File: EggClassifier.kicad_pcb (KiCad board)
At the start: 2 copper layers, 100 x 100 mm, 77 parts, among them J1 ST-LINK, J10 LCD_CHAR, J11 SERVO2, J12 BME280, J13 UART1, J14 FAN, J15 UART2, J16 AS7265X, J17 TFT_SPI, J2 USB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

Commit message: snapshot
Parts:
- C10, C11, C14, C15, C2, C5, C6, C7, C8, C9: footprint Capacitor_SMD:C_0805_2012Metric_Pad1.18x1.45mm_HandSolder -> EggClassifier:C_0805_2012Metric_Pad1.18x1.45mm_HandSolder
- C12, C13, C16, C17, C18, C19, C20, C21, C22: footprint Capacitor_SMD:C_0603_1608Metric_Pad1.08x0.95mm_HandSolder -> EggClassifier:C_0805_2012Metric_Pad1.18x1.45mm_HandSolder
- D1: footprint Diode_SMD:D_SMB_Handsoldering -> EggClassifier:D_SMB_Handsoldering
- D2, D3, D4: footprint Diode_SMD:D_SMA_Handsoldering -> EggClassifier:D_SMA_Handsoldering
- D5, D6: footprint LED_SMD:LED_0805_2012Metric_Pad1.15x1.40mm_HandSolder -> EggClassifier:LED_0805_2012Metric_Pad1.15x1.40mm_HandSolder
- H1, H2, H3, H4: footprint PCM_JLCPCB:Hole, 3mm -> EggClassifier:Hole, 3mm
- J1: footprint Connector_PinHeader_2.54mm:PinHeader_1x05_P2.54mm_Vertical -> EggClassifier:PinHeader_1x05_P2.54mm_Vertical
- J10, J12, J16, J2, J5: footprint Connector_PinHeader_2.54mm:PinHeader_1x04_P2.54mm_Vertical -> EggClassifier:PinHeader_1x04_P2.54mm_Vertical
- J11, J13, J14, J15, J8, J9: footprint Connector_PinHeader_2.54mm:PinHeader_1x03_P2.54mm_Vertical -> EggClassifier:PinHeader_1x03_P2.54mm_Vertical
- J17: footprint Connector_PinHeader_2.54mm:PinHeader_1x15_P2.54mm_Vertical -> EggClassifier:PinSocket_1x14_P2.54mm_Vertical
- J6: footprint Connector_PinHeader_2.54mm:PinHeader_2x09_P2.54mm_Vertical -> EggClassifier:PinHeader_2x09_P2.54mm_Vertical
- J7: footprint Connector_PinHeader_2.54mm:PinHeader_2x05_P2.54mm_Vertical -> EggClassifier:PinHeader_2x05_P2.54mm_Vertical
- Q1, Q2, Q3: footprint PCM_Package_TO_SOT_SMD_AKL:SOT-223-3_TabPin2 -> EggClassifier:SOT-223-3_TabPin2
- R1, R10, R11, R12, R13, R14, R15, R16, R17, R18, R19, R2, R20, R3, R4, R5, R6, R7, R8, R9: footprint Resistor_SMD:R_0805_2012Metric_Pad1.20x1.40mm_HandSolder -> EggClassifier:R_0805_2012Metric_Pad1.20x1.40mm_HandSolder
- SW1: footprint Button_Switch_THT:SW_PUSH_6mm_H4.3mm -> EggClassifier:SW_PUSH_6mm_H4.3mm
- U1: footprint LM2676S-3.3_NOPB:TO127P1435X464-8N -> EggClassifier:TO127P1435X464-8N
- U2: footprint Package_TO_SOT_SMD:SOT-223-3_TabPin2 -> EggClassifier:SOT-223-3_TabPin2
- U3: footprint Package_QFP:LQFP-100_14x14mm_P0.5mm -> EggClassifier:LQFP-100_14x14mm_P0.5mm
- U4: footprint PCM_JLCPCB:SOIC-8_L5.3-W5.3-P1.27-LS8.0-BL -> EggClassifier:SOIC-8_L5.3-W5.3-P1.27-LS8.0-BL
- Y1: footprint Oscillator:Oscillator_SMD_Abracon_ASV-4Pin_7.0x5.1mm_HandSoldering -> EggClassifier:Oscillator_SMD_Abracon_ASV-4Pin_7.0x5.1mm_HandSoldering
- moved R13 4.40 mm to (117.5, 69.0)
- moved R3 1.45 mm to (104.3, 55.8)
- moved R4 1.45 mm to (107.7, 55.8)
- moved J12 1.30 mm to (99.8, 51.4)
- moved J15 1.27 mm to (142.5, 51.4)
- moved C17 0.64 mm to (124.6, 72.3)
- moved C19 0.42 mm to (123.6, 96.6)
- moved C22 0.18 mm to (143.8, 77.5)
- moved C20 0.17 mm to (138.7, 98.0)
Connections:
- J7 pad 9: GND -> VCC
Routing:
- net UART2_TX: track 0.00 -> 76.0 mm, vias 0 -> 1
- net USER_GPIO4: track 0.00 -> 72.3 mm, vias 0 -> 3
- net USER_GPIO1: track 0.00 -> 55.0 mm, vias 0 -> 1
- net USER_GPIO2: track 0.00 -> 54.9 mm, vias 0 -> 1
- net USER_GPIO3: track 0.00 -> 54.3 mm, vias 0 -> 1
- net +3.3V: track 139.7 -> 159.2 mm, vias 5 -> 8
- net I2C1_SDA: track 47.2 -> 55.9 mm
- net I2C1_SCL: track 46.6 -> 54.2 mm
- net VCC: track 211.9 -> 218.9 mm
- net Net-(Y1-OUT): track 4.61 -> 9.26 mm
- net UART1_TX: track 49.5 -> 53.8 mm
- net Net-(U3-PH0): track 25.4 -> 22.1 mm
- net UART1_RX: track 47.6 -> 50.3 mm
- net GND: track 85.2 -> 87.8 mm
- net UART2_RX: track 33.3 -> 32.1 mm
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
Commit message: almost finsihed
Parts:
- moved R9 2.29 mm to (92.7, 61.6)
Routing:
- net ADC_IN2: track 0.00 -> 71.6 mm, vias 0 -> 1
- net ADC_IN1: track 0.00 -> 65.0 mm, vias 0 -> 1
- net I2C2_SDA: track 78.5 -> 105.9 mm
- net I2C2_SCL: track 79.3 -> 97.8 mm
- net +3.3V: track 159.2 -> 161.6 mm
- net I2C1_SDA: track 55.9 -> 55.2 mm

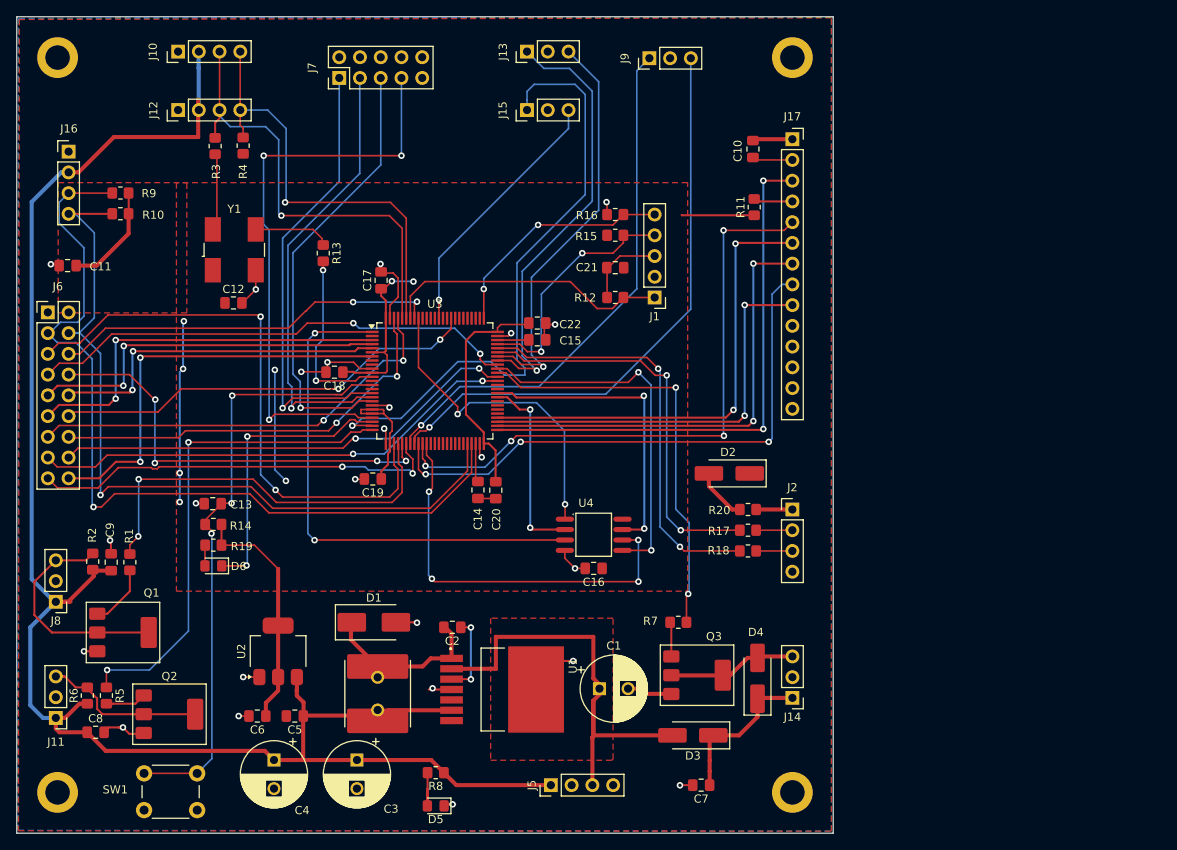
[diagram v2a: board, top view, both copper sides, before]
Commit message: complete PCB layout
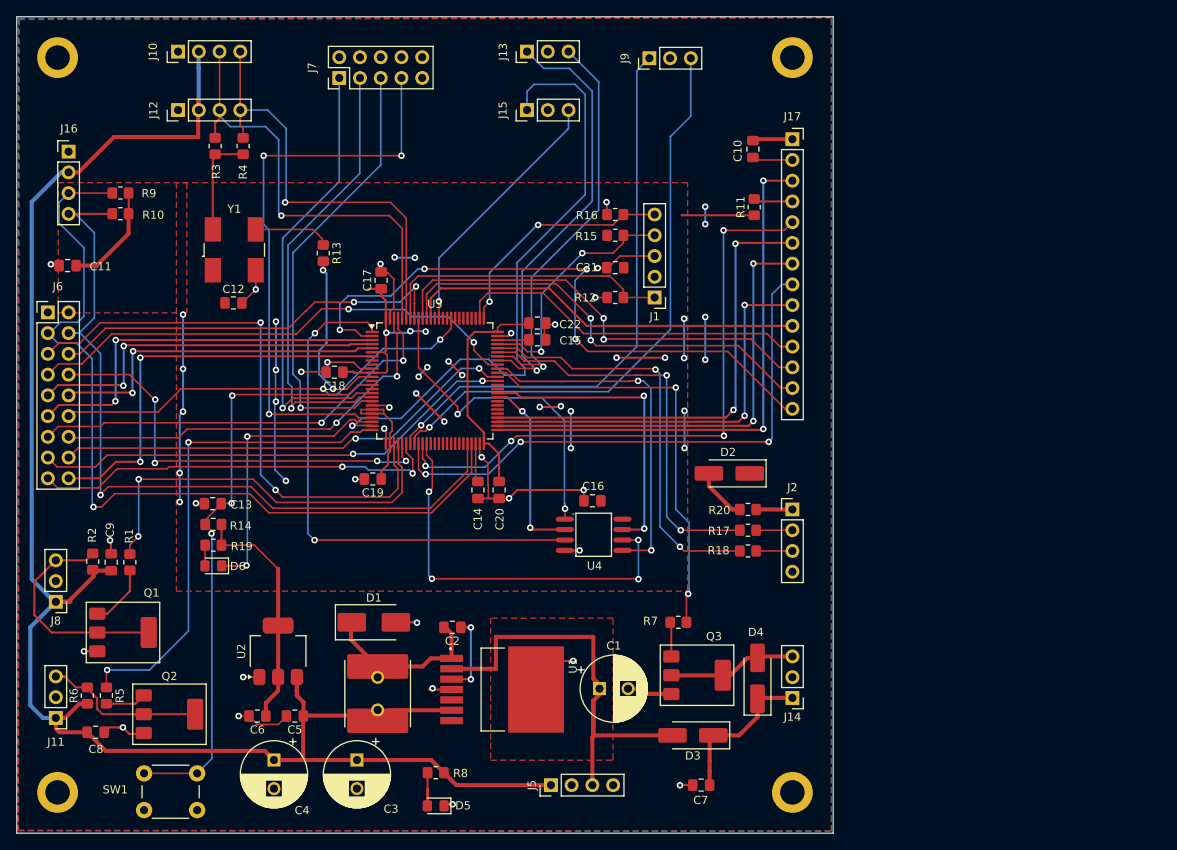
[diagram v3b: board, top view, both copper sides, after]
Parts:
- moved C16 8.28 mm to (150.5, 99.3)
- moved C20 0.41 mm to (139.1, 98.0)
- moved R4 0.05 mm to (107.7, 55.8)
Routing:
- net TFT_INT: track 0.00 -> 78.8 mm, vias 0 -> 4
- net SPI1_MOSI: track 0.00 -> 55.2 mm, vias 0 -> 2
- net SPI1_MISO: track 0.00 -> 55.1 mm, vias 0 -> 2
- net SPI1_SCK: track 0.00 -> 49.1 mm
- net SPI1_NCS: track 0.00 -> 43.5 mm
- net GND: track 87.8 -> 123.0 mm, vias 24 -> 36
- net +3.3V: track 161.6 -> 193.0 mm, vias 8 -> 22
- net VCC: track 218.7 -> 226.1 mm, vias 0 -> 4
- net ADC_IN1: track 65.0 -> 69.1 mm
- net CAM_VS: track 47.5 -> 50.0 mm
- net CAM_MCLK: track 60.2 -> 62.0 mm
- net /DevEBox/QSPI_D2: track 63.8 -> 65.1 mm
- net /DevEBox/QSPI_D0: track 44.5 -> 43.2 mm
- net /DevEBox/QSPI_NCS: track 39.7 -> 40.9 mm
- net CAM_HS: track 71.6 -> 70.4 mm
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
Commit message: more fine tuning
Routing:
- net UART2_TX: track 76.3 -> 70.6 mm
- net VCC: track 226.1 -> 231.2 mm, vias 4 -> 6
- net /DevEBox/QSPI_CLK: track 49.2 -> 46.7 mm
- net I2C2_SCL: track 97.8 -> 95.9 mm
- net I2C2_SDA: track 105.7 -> 103.9 mm
- net /DevEBox/QSPI_D3: track 37.2 -> 35.6 mm
- net /DevEBox/DM: track 48.9 -> 49.9 mm
- net /DevEBox/QSPI_D1: track 22.8 -> 21.9 mm
- net GND: track 123.0 -> 123.5 mm

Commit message: more fine tuning
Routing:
- net GND: track 123.5 -> 124.5 mm
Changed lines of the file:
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@@
 	)
 	(segment
+		(start 128.6918 85.8978)
+		(end 132.3748 89.5808)
+		(width 0.25)
+		(layer "F.Cu")
+		(net 1)
+	)
+	(segment
 		(start 156.9366 122.931)
 		(end 156.3016 122.296)
@@
 	)
 	(segment
-		(start 134.5592 83.8912)
-		(end 132.832 82.164)
-		(width 0.25)
-		(layer "F.Cu")
-		(net 1)
-	)
-	(segment
 		(start 129.022 114.2188)
 		(end 128.7172 114.2188)
@@
 	)
 	(segment
-		(start 132.3748 89.5808)
-		(end 128.9204 86.1264)
+		(start 132.832 82.164)
+		(end 134.5592 83.8912)
 		(width 0.25)
 		(layer "F.Cu")
@@
 	)
 	(segment
+		(start 128.5648 85.8978)
+		(end 128.6918 85.8978)
+		(width 0.25)
+		(layer "F.Cu")
+		(net 1)
+	)
+	(segment
 		(start 162.7925 134.112)
 		(end 161.2496 134.112)
@@
 	)
 	(segment
-		(start 132.832 82.164)
-		(end 132.7558 82.164)
-		(width 0.25)
-		(layer "F.Cu")
-		(net 1)
-	)
-	(segment
 		(start 137.7596 94.7624)
 		(end 137.7596 99.0003)
@@
 	)
 	(segment
+		(start 128.4378 85.7708)
+		(end 128.5648 85.8978)
+		(width 0.25)
+		(layer "F.Cu")
+		(net 1)
+	)
+	(segment
+		(start 132.8066 82.164)
+		(end 132.832 82.164)
+		(width 0.25)
+		(layer "F.Cu")
+		(net 1)
+	)
+	(segment
 		(start 140.2781 99.0003)
 		(end 140.2996 98.9788)
@@
 	)
 	(segment
+		(start 132.4764 81.8338)
+		(end 132.8066 82.164)
+		(width 0.25)
+		(layer "F.Cu")
+		(net 1)
+	)
+	(segment
 		(start 133.731 136.462)
 		(end 132.153 136.462)
@@
 	)
 	(via
-		(at 128.9204 86.1264)
+		(at 128.4378 85.7708)
 		(size 0.8)
 		(drill 0.4)
@@
 	)
 	(via
-		(at 132.7558 82.164)
+		(at 132.4764 81.8338)
 		(size 0.8)
 		(drill 0.4)
@@
 	)
 	(segment
-		(start 124.8818 93.5432)
+		(start 121.1988 93.5432)
+		(end 121.9608 92.7812)
+		(width 0.2)
+		(layer "B.Cu")
+		(net 35)
+	)
+	(segment
+		(start 125.6438 92.7812)
 		(end 133.7718 84.6532)
 		(width 0.2)
@@
 	)
 	(segment
-		(start 121.1988 93.5432)
-		(end 124.8818 93.5432)
+		(start 121.9608 92.7812)
+		(end 125.6438 92.7812)
 		(width 0.2)
 		(layer "B.Cu")
@@
 	)
 	(segment
-		(start 127.0662 89.1998)
-		(end 134.4322 81.8338)
+		(start 139.055 81.5544)
+		(end 141.3664 79.243)
 		(width 0.2)
 		(layer "B.Cu")
@@
 	)
 	(segment
-		(start 121.096875 90.088475)
-		(end 121.351525 90.088475)
+		(start 142.484 50.16)
+		(end 142.499 50.175)
 		(width 0.2)
 		(layer "B.Cu")
@@
 	)
 	(segment
-		(start 142.484 50.16)
-		(end 142.499 50.175)
+		(start 149.6214 49.525)
+		(end 148.3768 48.2804)
 		(width 0.2)
 		(layer "B.Cu")
@@
 	)
 	(segment
-		(start 142.499 50.175)
-		(end 142.499 51.43)
+		(start 149.6214 62.6568)
+		(end 149.6214 49.525)
 		(width 0.2)
 		(layer "B.Cu")
@@
 	)
 	(segment
-		(start 148.3768 48.2804)
-		(end 143.373 48.2804)
+		(start 121.7322 89.4792)
+		(end 126.3296 89.4792)
 		(width 0.2)
 		(layer "B.Cu")
@@
 	)
 	(segment
-		(start 149.6214 62.6568)
-		(end 149.6214 49.525)
+		(start 142.499 50.175)
+		(end 142.499 51.43)
 		(width 0.2)
 		(layer "B.Cu")
@@
 	)
 	(segment
-		(start 149.6214 49.525)
-		(end 148.3768 48.2804)
+		(start 143.373 48.2804)
+		(end 142.499 49.1544)
 		(width 0.2)
 		(layer "B.Cu")
@@
 	)
 	(segment
-		(start 134.4322 81.8338)
-		(end 138.7756 81.8338)
+		(start 142.499 49.1544)
+		(end 142.499 50.16)
 		(width 0.2)
 		(layer "B.Cu")
@@
 	)
 	(segment
-		(start 122.2402 89.1998)
-		(end 127.0662 89.1998)
+		(start 121.122925 90.088475)
+		(end 121.7322 89.4792)
 		(width 0.2)
 		(layer "B.Cu")
@@
 	)
 	(segment
-		(start 141.3664 79.243)
-		(end 141.3664 70.9118)
+		(start 121.096875 90.088475)
+		(end 121.122925 90.088475)
 		(width 0.2)
 		(layer "B.Cu")
@@
 	)
 	(segment
-		(start 142.499 50.16)
-		(end 142.484 50.16)
+		(start 141.3664 79.243)
+		(end 141.3664 70.9118)
 		(width 0.2)
 		(layer "B.Cu")
@@
 	)
 	(segment
-		(start 142.499 49.1544)
-		(end 142.499 50.16)
+		(start 134.2544 81.5544)
+		(end 139.055 81.5544)
 		(width 0.2)
 		(layer "B.Cu")
@@
 	)
 	(segment
-		(start 121.351525 90.088475)
-		(end 122.2402 89.1998)
+		(start 148.3768 48.2804)
+		(end 143.373 48.2804)
 		(width 0.2)
 		(layer "B.Cu")
@@
 	)
 	(segment
-		(start 138.7756 81.8338)
-		(end 141.3664 79.243)
+		(start 142.499 50.16)
+		(end 142.484 50.16)
 		(width 0.2)
 		(layer "B.Cu")
@@
 	)
 	(segment
-		(start 143.373 48.2804)
-		(end 142.499 49.1544)
+		(start 126.3296 89.4792)
+		(end 134.2544 81.5544)
 		(width 0.2)
 		(layer "B.Cu")

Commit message: yet more tweaks
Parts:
- J5: footprint EggClassifier:PinHeader_1x04_P2.54mm_Vertical -> EggClassifier:TerminalBlock_Xinya_XY308-2.54-4P_1x04_P2.54mm_Horizontal
- moved C12 9.17 mm to (105.9, 65.9)
- moved Y1 3.57 mm to (105.9, 72.0)
- moved R13 2.80 mm to (117.9, 71.7)
- turned J5 to 0 degrees
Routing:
- net VCC: track 231.2 -> 214.8 mm, vias 6 -> 7
- net Net-(J11-Pin_3): track 22.4 -> 25.4 mm, vias 0 -> 1
- net Net-(U3-PH0): track 22.3 -> 19.4 mm
- net USER_GPIO1: track 55.0 -> 53.6 mm
- net GND: track 124.5 -> 123.2 mm, vias 36 -> 37
- net CAM_HS: track 70.4 -> 69.5 mm
- net Net-(Q2-B): track 4.28 -> 4.99 mm
- net Net-(Y1-OUT): track 9.26 -> 9.96 mm
- net Net-(J8-Pin_3): vias 0 -> 1

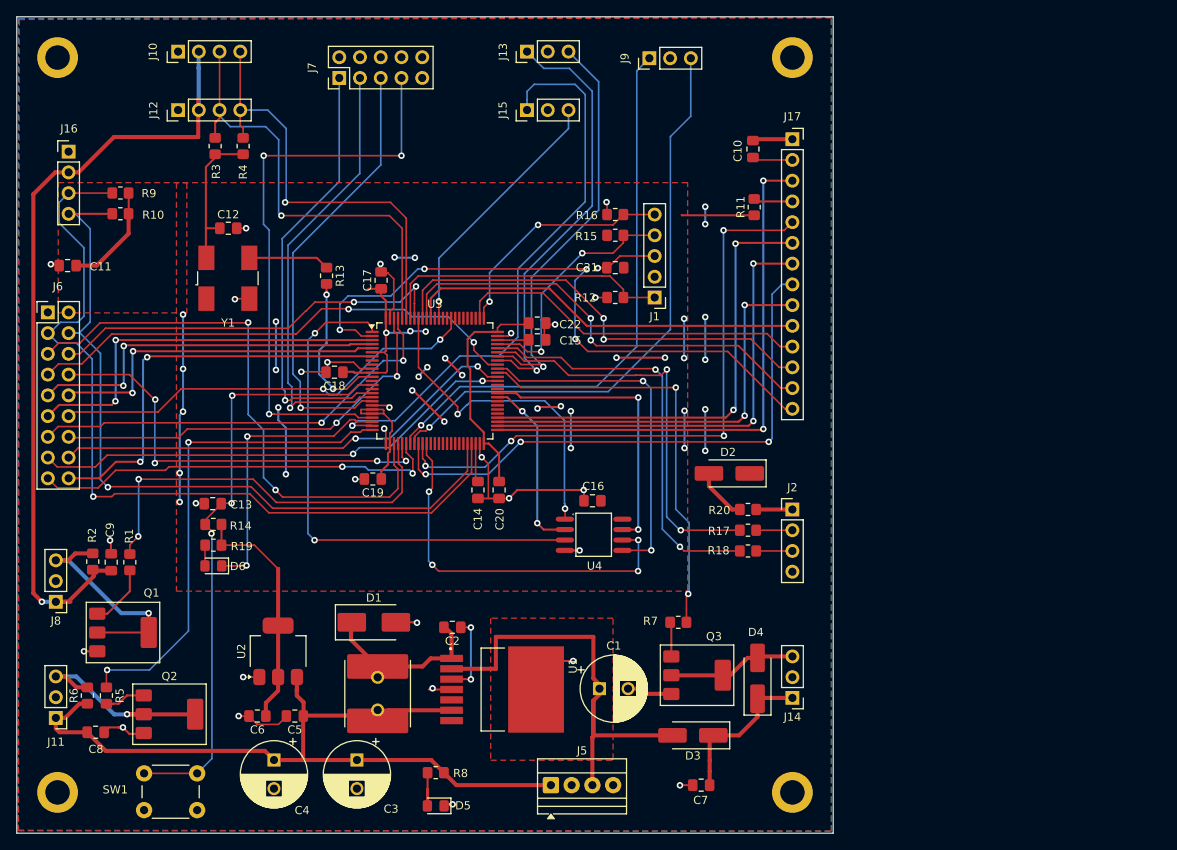
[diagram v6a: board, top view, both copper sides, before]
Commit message: change board to dimensions 120mm x 80mm
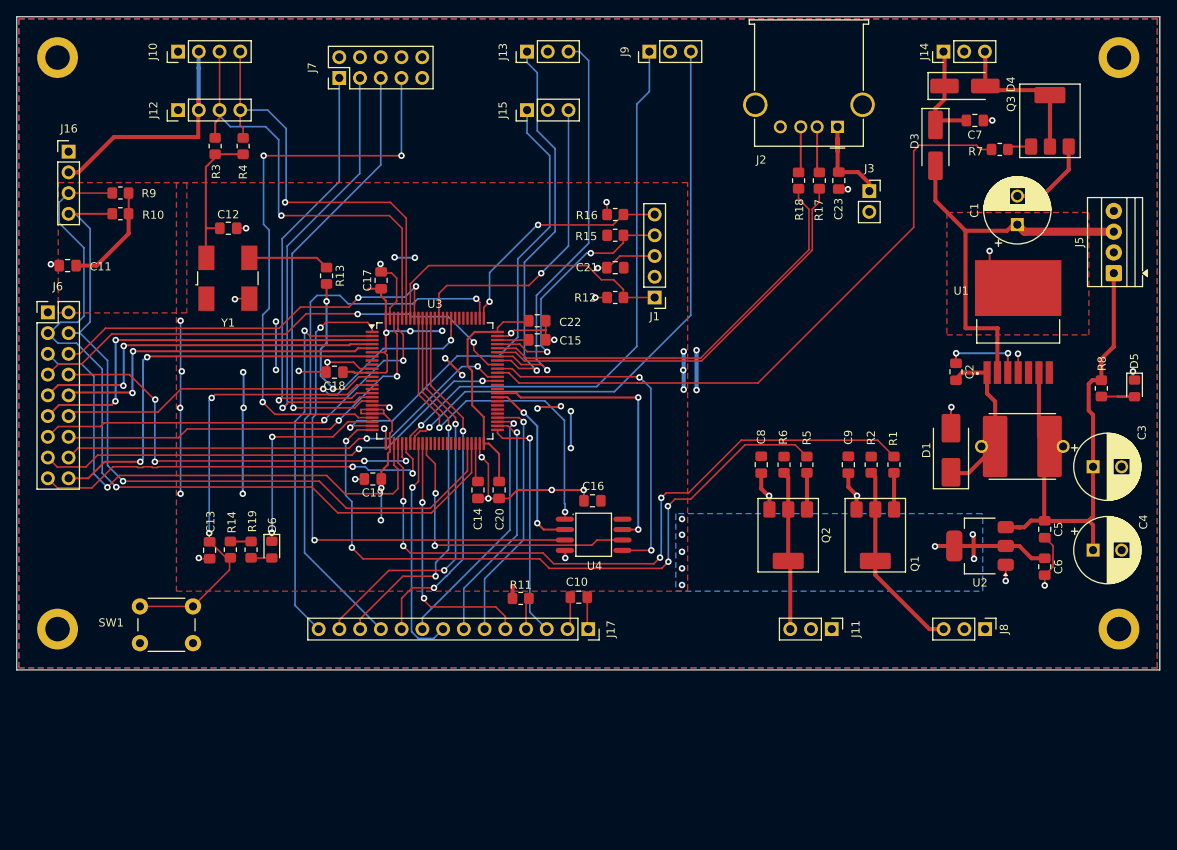
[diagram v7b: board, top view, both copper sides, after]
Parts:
- removed D2: SS36, EggClassifier:D_SMA_Handsoldering
- removed R20: 0, EggClassifier:R_0805_2012Metric_Pad1.20x1.40mm_HandSolder
- added C23: 104, EggClassifier:C_0805_2012Metric_Pad1.18x1.45mm_HandSolder, F.Cu at (180.7, 60.1)
- added J3: Jumper, EggClassifier:PinSocket_1x02_P2.54mm_Vertical, F.Cu at (184.4, 61.4)
- J2: value USB -> USB_A; footprint EggClassifier:PinHeader_1x04_P2.54mm_Vertical -> EggClassifier:USB_A_Molex_67643_Horizontal
- moved J8 113.9 mm to (198.6, 115.0), turned to -90 degrees
- moved C4 103.6 mm to (211.8, 105.3), turned to 0 degrees
- moved D5 99.7 mm to (216.9, 85.5), turned to -90 degrees
- moved C6 98.1 mm to (205.9, 107.4), turned to -90 degrees
- moved C3 97.1 mm to (211.8, 95.1), turned to 0 degrees
- moved R2 96.1 mm to (184.6, 94.9), turned to -90 degrees
- moved J11 95.7 mm to (179.8, 115.0), turned to -90 degrees
- moved C5 94.6 mm to (205.9, 102.8), turned to -90 degrees
- moved R1 94.3 mm to (187.4, 94.9)
- moved R8 94.1 mm to (212.8, 85.5), turned to -90 degrees
- moved J5 93.2 mm to (214.4, 71.4), turned to 90 degrees
- moved Q1 92.9 mm to (185.2, 103.5), turned to -90 degrees
- moved C9 91.1 mm to (181.9, 94.9), turned to -90 degrees
- moved R5 90.3 mm to (176.8, 94.9)
- moved R6 89.9 mm to (174.0, 94.9), turned to -90 degrees
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- renumbered R18 to R17, R17 to R18
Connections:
- J2 pad 1: Net-(J2-Pin_1) -> +5V
- J2 pad 2: Net-(J2-Pin_2) -> Net-(J2-D-)
- J2 pad 3: Net-(J2-Pin_3) -> Net-(J2-D+)
- R17 pad 1: /DevEBox/DP -> /DevEBox/DM
- R17 pad 2: Net-(J2-Pin_3) -> Net-(J2-D-)
- R18 pad 1: /DevEBox/DM -> /DevEBox/DP
- R18 pad 2: Net-(J2-Pin_2) -> Net-(J2-D+)
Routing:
- net VCC: track 214.8 -> 104.0 mm, vias 7 -> 2
- net TFT_RS: track 75.1 -> 31.6 mm, vias 4 -> 2
- net TFT_BL: track 69.2 -> 28.1 mm, vias 3 -> 1
- net SPI2_NCS: track 66.6 -> 28.9 mm, vias 2 -> 1
- net SERVO_OUT1: track 49.7 -> 85.1 mm, vias 2 -> 4
- net TFT_INT: track 78.8 -> 46.8 mm, vias 4 -> 1
- net FAN_OUT: track 52.1 -> 78.8 mm, vias 2 -> 0
- net SPI2_SCK: track 55.7 -> 29.5 mm, vias 2 -> 1
- net SPI2_MOSI: track 56.8 -> 30.8 mm, vias 2 -> 1
- net SPI1_NCS: track 43.5 -> 68.1 mm, vias 0 -> 1
- net SERVO_OUT2: track 60.3 -> 84.9 mm, vias 2 -> 4
- net SPI2_MISO: track 50.0 -> 31.9 mm, vias 2 -> 1
- net Net-(SW1-B): track 72.9 -> 55.0 mm, vias 3 -> 2
- net UART2_TX: track 70.6 -> 58.6 mm
- net +3.3V: track 192.9 -> 181.0 mm, vias 22 -> 29
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- added copper zone on B.Cu, net +3.3V
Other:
- board size 100 x 100 mm -> 140 x 80 mm
